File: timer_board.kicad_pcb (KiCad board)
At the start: 2 copper layers, 127 x 76.2 mm, 53 parts, among them IC1 ATMEGA32U4, K1 T9AS5D22-5, P1 USBMICRO, P2 OUT_INV, P3 Trigger, P4 OUT, Q1 NPN, Q2 NPN, U1 DS3231MZ, U2 74HC04, Y1 RESONATORSMD

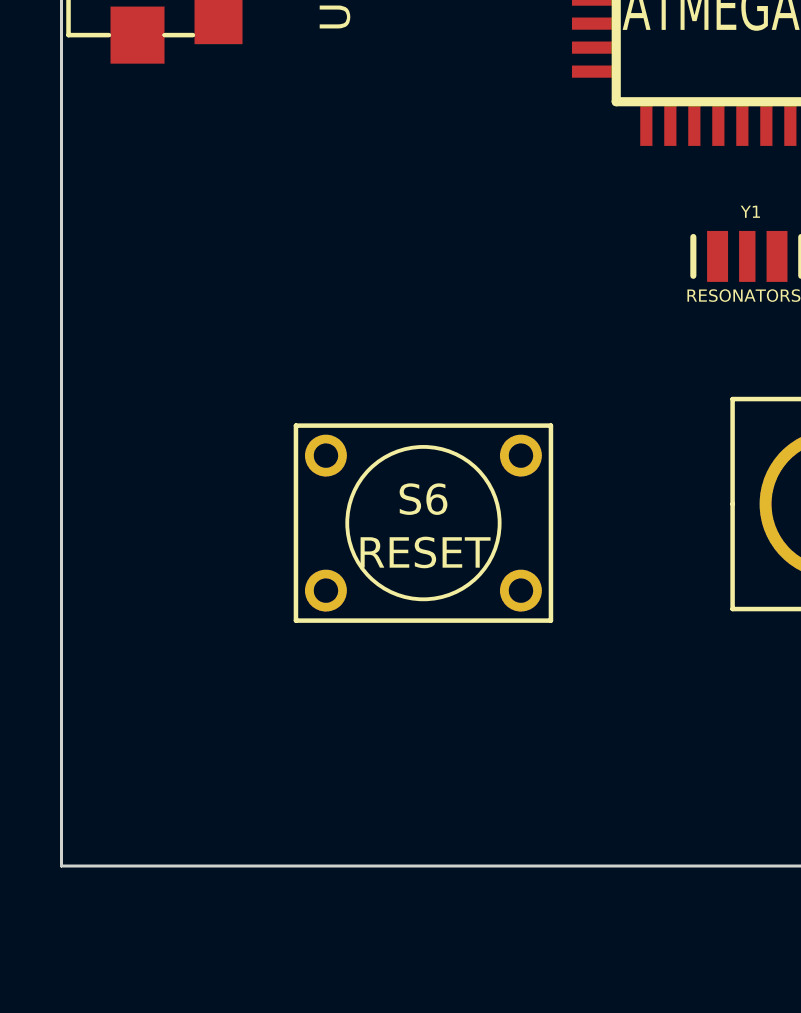
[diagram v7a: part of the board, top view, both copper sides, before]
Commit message: Added AVR ISP header
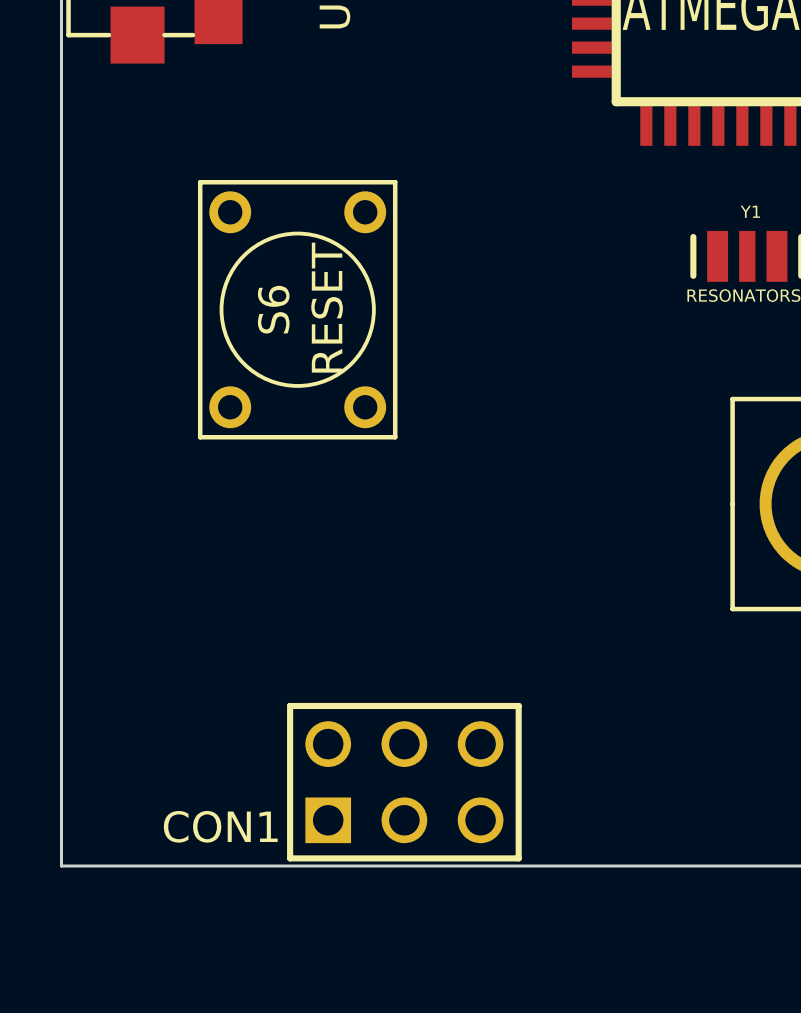
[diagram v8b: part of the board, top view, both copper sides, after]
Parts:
- added CON1: AVR-ISP-6, pin_array_3x2, F.Cu at (36.8, 98.8)
- moved S6 8.25 mm to (33.3, 83.1), turned to 90 degrees
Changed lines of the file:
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@@
 (kicad_pcb (version 3) (host pcbnew "(2013-05-16 BZR 4016)-stable")
   (general
-    (links 138)
-    (no_connects 138)
+    (links 144)
+    (no_connects 144)
     (area 25.349999 25.349999 152.450001 101.650001)
     (thickness 1.6)
@@
     (tracks 0)
     (zones 0)
-    (modules 53)
+    (modules 54)
     (nets 48)
   )
@@
   )
   (module SW_PUSH_6X6 (layer F.Cu)
-    (at 37.465 90.17)
-    (fp_text reference S6 (at 0 -0.762) (layer F.SilkS)
+    (at 33.274 83.058 90)
+    (fp_text reference S6 (at 0 -0.762 90) (layer F.SilkS)
       (effects (font (size 1.016 1.016) (thickness 0.2032)))
     )
-    (fp_text value RESET (at 0 1.016) (layer F.SilkS)
+    (fp_text value RESET (at 0 1.016 90) (layer F.SilkS)
+      (effects (font (size 1.016 1.016) (thickness 0.2032)))
+    )
+    (fp_line (start -4.25 3.25) (end -4.25 -3.25) (layer F.SilkS) (width 0.15))
+    (fp_line (start -4.25 -3.25) (end 4.25 -3.25) (layer F.SilkS) (width 0.15))
+    (fp_line (start 4.25 -3.25) (end 4.25 3.25) (layer F.SilkS) (width 0.15))
+    (fp_line (start 4.25 3.25) (end -4.25 3.25) (layer F.SilkS) (width 0.15))
+    (fp_circle (center 0 0) (end 0 -2.54) (layer F.SilkS) (width 0.127))
+    (pad 2 thru_hole circle (at 3.25 -2.25 90) (size 1.397 1.397) (drill 0.8128)
+      (layers *.Cu *.Mask F.SilkS)
+      (net 9 GND)
+    )
+    (pad 4 thru_hole circle (at 3.25 2.25 90) (size 1.397 1.397) (drill 0.8128)
+      (layers *.Cu *.Mask F.SilkS)
+      (net 47 reset)
+    )
+    (pad 1 thru_hole circle (at -3.25 -2.25 90) (size 1.397 1.397) (drill 0.8128)
+      (layers *.Cu *.Mask F.SilkS)
+      (net 9 GND)
+    )
+    (pad 3 thru_hole circle (at -3.25 2.25 90) (size 1.397 1.397) (drill 0.8128)
+      (layers *.Cu *.Mask F.SilkS)
+      (net 47 reset)
+    )
+  )
+  (module SW_PUSH_6X6 (layer F.Cu)
+    (at 93.98 68.58)
+    (fp_text reference S1 (at 0 -0.762) (layer F.SilkS)
+      (effects (font (size 1.016 1.016) (thickness 0.2032)))
+    )
+    (fp_text value UP (at 0 1.016) (layer F.SilkS)
       (effects (font (size 1.016 1.016) (thickness 0.2032)))
     )
@@
     (pad 2 thru_hole circle (at 3.25 -2.25) (size 1.397 1.397) (drill 0.8128)
       (layers *.Cu *.Mask F.SilkS)
-      (net 9 GND)
+      (net 45 UP)
     )
     (pad 4 thru_hole circle (at 3.25 2.25) (size 1.397 1.397) (drill 0.8128)
       (layers *.Cu *.Mask F.SilkS)
-      (net 47 reset)
+      (net 9 GND)
     )
     (pad 1 thru_hole circle (at -3.25 -2.25) (size 1.397 1.397) (drill 0.8128)
       (layers *.Cu *.Mask F.SilkS)
-      (net 9 GND)
+      (net 45 UP)
     )
     (pad 3 thru_hole circle (at -3.25 2.25) (size 1.397 1.397) (drill 0.8128)
       (layers *.Cu *.Mask F.SilkS)
-      (net 47 reset)
+      (net 9 GND)
     )
   )
   (module SW_PUSH_6X6 (layer F.Cu)
-    (at 93.98 68.58)
-    (fp_text reference S1 (at 0 -0.762) (layer F.SilkS)
+    (at 93.98 88.265)
+    (fp_text reference S2 (at 0 -0.762) (layer F.SilkS)
       (effects (font (size 1.016 1.016) (thickness 0.2032)))
     )
-    (fp_text value UP (at 0 1.016) (layer F.SilkS)
+    (fp_text value DOWN (at 0 1.016) (layer F.SilkS)
       (effects (font (size 1.016 1.016) (thickness 0.2032)))
     )
@@
     (pad 2 thru_hole circle (at 3.25 -2.25) (size 1.397 1.397) (drill 0.8128)
       (layers *.Cu *.Mask F.SilkS)
-      (net 45 UP)
+      (net 7 Down)
     )
     (pad 4 thru_hole circle (at 3.25 2.25) (size 1.397 1.397) (drill 0.8128)
@@
     (pad 1 thru_hole circle (at -3.25 -2.25) (size 1.397 1.397) (drill 0.8128)
       (layers *.Cu *.Mask F.SilkS)
-      (net 45 UP)
+      (net 7 Down)
     )
     (pad 3 thru_hole circle (at -3.25 2.25) (size 1.397 1.397) (drill 0.8128)
@@
   )
   (module SW_PUSH_6X6 (layer F.Cu)
-    (at 93.98 88.265)
-    (fp_text reference S2 (at 0 -0.762) (layer F.SilkS)
+    (at 125.73 78.74)
+    (fp_text reference S5 (at 0 -0.762) (layer F.SilkS)
       (effects (font (size 1.016 1.016) (thickness 0.2032)))
     )
-    (fp_text value DOWN (at 0 1.016) (layer F.SilkS)
+    (fp_text value SELECT (at 0 1.016) (layer F.SilkS)
       (effects (font (size 1.016 1.016) (thickness 0.2032)))
     )
@@
     (pad 2 thru_hole circle (at 3.25 -2.25) (size 1.397 1.397) (drill 0.8128)
       (layers *.Cu *.Mask F.SilkS)
-      (net 7 Down)
+      (net 44 Select)
     )
     (pad 4 thru_hole circle (at 3.25 2.25) (size 1.397 1.397) (drill 0.8128)
@@
     (pad 1 thru_hole circle (at -3.25 -2.25) (size 1.397 1.397) (drill 0.8128)
       (layers *.Cu *.Mask F.SilkS)
-      (net 7 Down)
+      (net 44 Select)
     )
     (pad 3 thru_hole circle (at -3.25 2.25) (size 1.397 1.397) (drill 0.8128)
@@
   )
   (module SW_PUSH_6X6 (layer F.Cu)
-    (at 125.73 78.74)
-    (fp_text reference S5 (at 0 -0.762) (layer F.SilkS)
+    (at 102.87 78.74)
+    (fp_text reference S4 (at 0 -0.762) (layer F.SilkS)
       (effects (font (size 1.016 1.016) (thickness 0.2032)))
     )
-    (fp_text value SELECT (at 0 1.016) (layer F.SilkS)
+    (fp_text value RIGHT (at 0 1.016) (layer F.SilkS)
       (effects (font (size 1.016 1.016) (thickness 0.2032)))
     )
@@
     (pad 2 thru_hole circle (at 3.25 -2.25) (size 1.397 1.397) (drill 0.8128)
       (layers *.Cu *.Mask F.SilkS)
-      (net 44 Select)
+      (net 41 Right)
     )
     (pad 4 thru_hole circle (at 3.25 2.25) (size 1.397 1.397) (drill 0.8128)
@@
     (pad 1 thru_hole circle (at -3.25 -2.25) (size 1.397 1.397) (drill 0.8128)
       (layers *.Cu *.Mask F.SilkS)
-      (net 44 Select)
+      (net 41 Right)
     )
     (pad 3 thru_hole circle (at -3.25 2.25) (size 1.397 1.397) (drill 0.8128)
@@
   )
   (module SW_PUSH_6X6 (layer F.Cu)
-    (at 102.87 78.74)
-    (fp_text reference S4 (at 0 -0.762) (layer F.SilkS)
+    (at 85.09 78.105)
+    (fp_text reference S3 (at 0 -0.762) (layer F.SilkS)
       (effects (font (size 1.016 1.016) (thickness 0.2032)))
     )
-    (fp_text value RIGHT (at 0 1.016) (layer F.SilkS)
+    (fp_text value LEFT (at 0 1.016) (layer F.SilkS)
       (effects (font (size 1.016 1.016) (thickness 0.2032)))
     )
@@
     (pad 2 thru_hole circle (at 3.25 -2.25) (size 1.397 1.397) (drill 0.8128)
       (layers *.Cu *.Mask F.SilkS)
-      (net 41 Right)
+      (net 10 Left)
     )
     (pad 4 thru_hole circle (at 3.25 2.25) (size 1.397 1.397) (drill 0.8128)
@@
     (pad 1 thru_hole circle (at -3.25 -2.25) (size 1.397 1.397) (drill 0.8128)
       (layers *.Cu *.Mask F.SilkS)
-      (net 41 Right)
+      (net 10 Left)
     )
     (pad 3 thru_hole circle (at -3.25 2.25) (size 1.397 1.397) (drill 0.8128)
@@
     )
   )
-  (module SW_PUSH_6X6 (layer F.Cu)
-    (at 85.09 78.105)
-    (fp_text reference S3 (at 0 -0.762) (layer F.SilkS)
+  (module pin_array_3x2 (layer F.Cu)
+    (at 36.83 98.806)
+    (descr "Double rangee de contacts 2 x 4 pins")
+    (tags CONN)
+    (fp_text reference CON1 (at -6.096 1.524) (layer F.SilkS)
       (effects (font (size 1.016 1.016) (thickness 0.2032)))
     )
-    (fp_text value LEFT (at 0 1.016) (layer F.SilkS)
+    (fp_text value AVR-ISP-6 (at 0.254 -3.81) (layer F.SilkS) hide
       (effects (font (size 1.016 1.016) (thickness 0.2032)))
     )
-    (fp_line (start -4.25 3.25) (end -4.25 -3.25) (layer F.SilkS) (width 0.15))
-    (fp_line (start -4.25 -3.25) (end 4.25 -3.25) (layer F.SilkS) (width 0.15))
-    (fp_line (start 4.25 -3.25) (end 4.25 3.25) (layer F.SilkS) (width 0.15))
-    (fp_line (start 4.25 3.25) (end -4.25 3.25) (layer F.SilkS) (width 0.15))
-    (fp_circle (center 0 0) (end 0 -2.54) (layer F.SilkS) (width 0.127))
-    (pad 2 thru_hole circle (at 3.25 -2.25) (size 1.397 1.397) (drill 0.8128)
-      (layers *.Cu *.Mask F.SilkS)
-      (net 10 Left)
-    )
-    (pad 4 thru_hole circle (at 3.25 2.25) (size 1.397 1.397) (drill 0.8128)
-      (layers *.Cu *.Mask F.SilkS)
-      (net 9 GND)
-    )
-    (pad 1 thru_hole circle (at -3.25 -2.25) (size 1.397 1.397) (drill 0.8128)
-      (layers *.Cu *.Mask F.SilkS)
-      (net 10 Left)
-    )
-    (pad 3 thru_hole circle (at -3.25 2.25) (size 1.397 1.397) (drill 0.8128)
-      (layers *.Cu *.Mask F.SilkS)
-      (net 9 GND)
-    )
-  )
+    (fp_line (start 3.81 2.54) (end -3.81 2.54) (layer F.SilkS) (width 0.2032))
+    (fp_line (start -3.81 -2.54) (end 3.81 -2.54) (layer F.SilkS) (width 0.2032))
+    (fp_line (start 3.81 -2.54) (end 3.81 2.54) (layer F.SilkS) (width 0.2032))
+    (fp_line (start -3.81 2.54) (end -3.81 -2.54) (layer F.SilkS) (width 0.2032))
+    (pad 1 thru_hole rect (at -2.54 1.27) (size 1.524 1.524) (drill 1.016)
+      (layers *.Cu *.Mask F.SilkS)
+      (net 17 N-000018)
+    )
+    (pad 2 thru_hole circle (at -2.54 -1.27) (size 1.524 1.524) (drill 1.016)
+      (layers *.Cu *.Mask F.SilkS)
+      (net 1 +5V)
+    )
+    (pad 3 thru_hole circle (at 0 1.27) (size 1.524 1.524) (drill 1.016)
+      (layers *.Cu *.Mask F.SilkS)
+      (net 20 N-000021)
+    )
+    (pad 4 thru_hole circle (at 0 -1.27) (size 1.524 1.524) (drill 1.016)
+      (layers *.Cu *.Mask F.SilkS)
+      (net 21 N-000022)
+    )
+    (pad 5 thru_hole circle (at 2.54 1.27) (size 1.524 1.524) (drill 1.016)
+      (layers *.Cu *.Mask F.SilkS)
+      (net 47 reset)
+    )
+    (pad 6 thru_hole circle (at 2.54 -1.27) (size 1.524 1.524) (drill 1.016)
+      (layers *.Cu *.Mask F.SilkS)
+      (net 9 GND)
+    )
+    (model pin_array/pins_array_3x2.wrl
+      (at (xyz 0 0 0))
+      (scale (xyz 1 1 1))
+      (rotate (xyz 0 0 0))
+    )
+  )
